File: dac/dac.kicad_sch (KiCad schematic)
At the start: 30 parts, among them J1 USB_B, U1 PCM2902, U2 SPX3819M5-L, Y1 12MHz

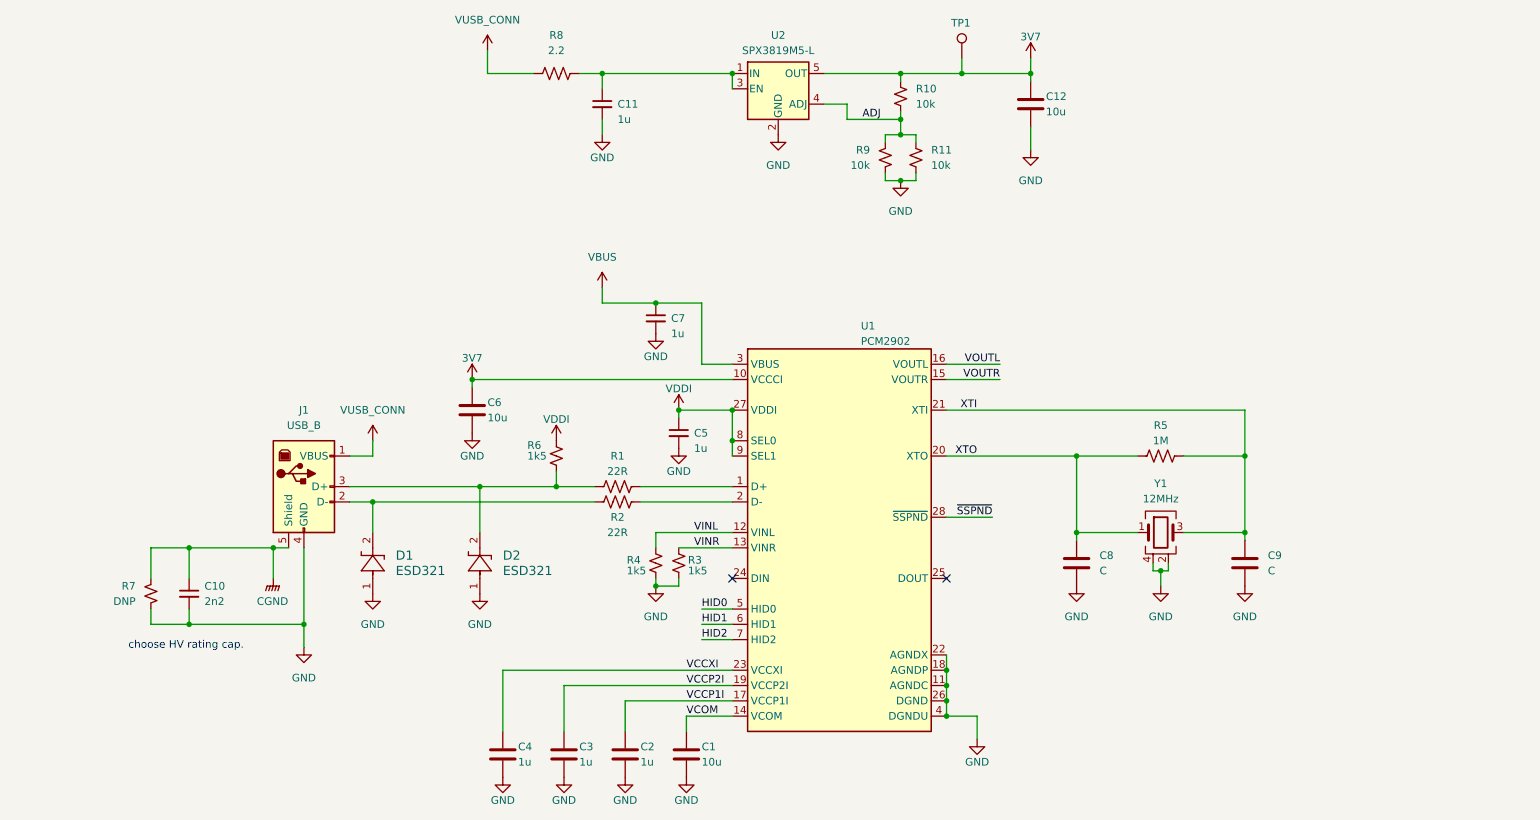
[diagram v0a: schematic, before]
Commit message: finished component placement, need to figure out header pinouts
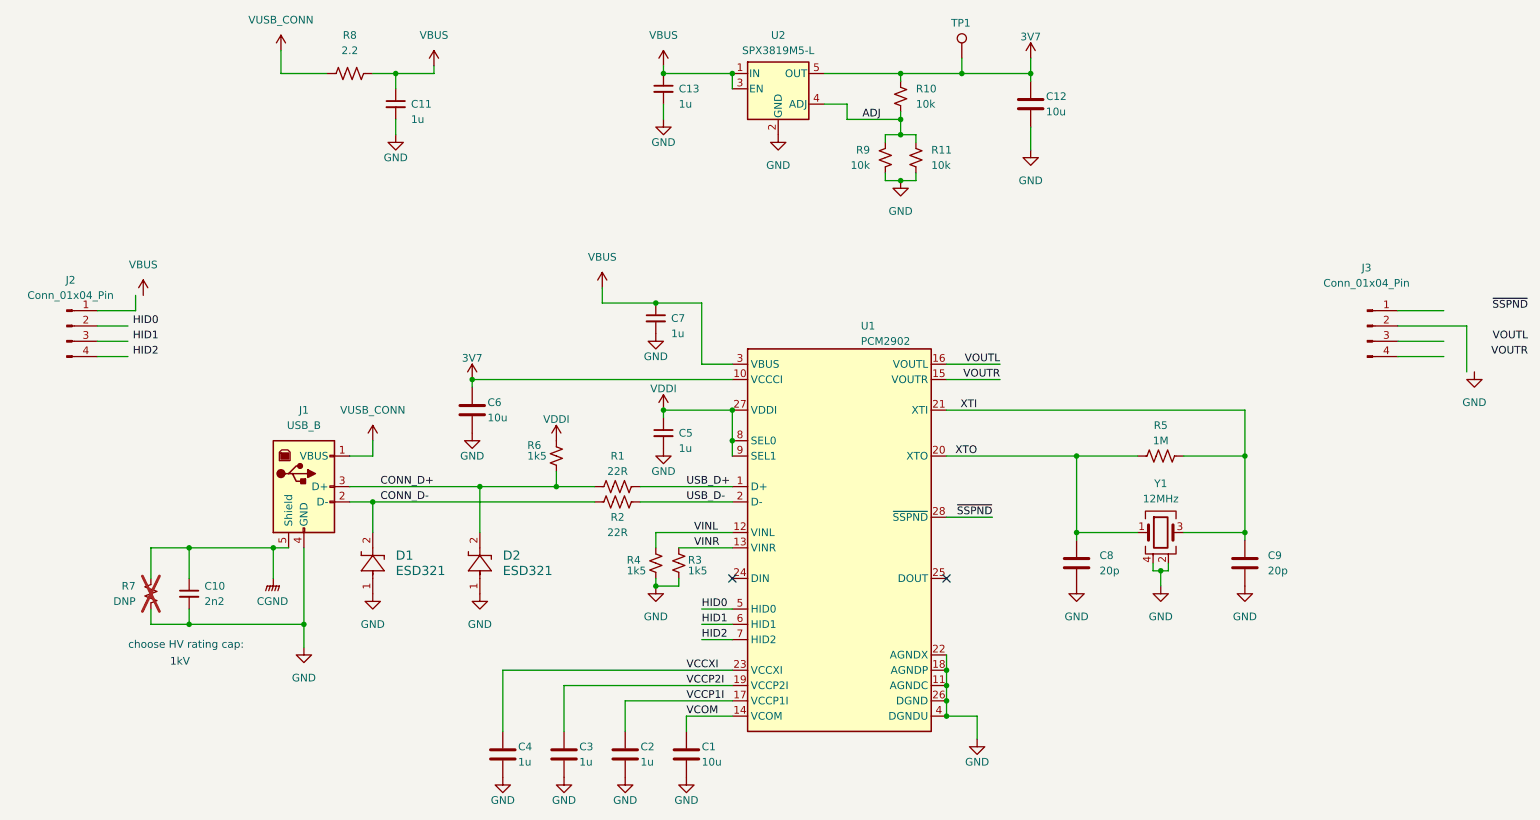
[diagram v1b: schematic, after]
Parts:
- added C13: 1u, Capacitor_SMD:C_0402_1005Metric_Pad0.74x0.62mm_HandSolder, symbol Device:C_Small
- added J2, J3: Conn_01x04_Pin, Connector_PinHeader_2.54mm:PinHeader_1x04_P2.54mm_Vertical, symbol Connector:Conn_01x04_Pin
- C1, C10, C12, C6: footprint (none) -> Capacitor_SMD:C_0805_2012Metric_Pad1.18x1.45mm_HandSolder
- C11, C2, C3, C4, C5, C7: footprint (none) -> Capacitor_SMD:C_0402_1005Metric_Pad0.74x0.62mm_HandSolder
- C8, C9: value C -> 20p; footprint (none) -> Capacitor_SMD:C_0402_1005Metric_Pad0.74x0.62mm_HandSolder
- J1: footprint (none) -> Connector_USB:USB_B_OST_USB-B1HSxx_Horizontal
- R1, R10, R11, R2, R3, R4, R5, R6, R9: footprint (none) -> Resistor_SMD:R_0402_1005Metric_Pad0.72x0.64mm_HandSolder
- R7: footprint (none) -> Resistor_SMD:R_0402_1005Metric_Pad0.72x0.64mm_HandSolder; now not fitted
- R8: footprint (none) -> Resistor_SMD:R_0603_1608Metric_Pad0.98x0.95mm_HandSolder
- TP1: footprint (none) -> TestPoint:TestPoint_Pad_D1.0mm
- Y1: footprint (none) -> ABM8:XTAL_ABM8-12.000MHZ-12-B1U-T
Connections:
- net GND: now also C13.2
- net VBUS: now also C11.1, R8.2, U2.1 (IN), U2.3 (EN), C13.1
- net USB_D+: now reaches R1.2, U1.1 (D+)
- net USB_D-: now reaches R2.2, U1.2 (D-)
- net CONN_D-: now reaches D1.2, J1.2 (D-), R2.1
- net CONN_D+: now reaches D2.2, J1.3 (D+), R1.1, R6.2
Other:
- note added: "1kV"
- note added: "choose HV rating cap:"
- note removed: "choose HV rating cap."
- moved on the sheet: C11, C5, R8

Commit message: layout is complete
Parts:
- added TP2: TestPoint, TestPoint:TestPoint_Pad_D1.0mm, symbol Connector:TestPoint
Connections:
- net GND: now also J2.2 (Pin_2)
- net HID0: now also J3.1 (Pin_1)
- net HID1: now also J3.2 (Pin_2)
- net HID2: now also J3.3 (Pin_3)
- net VBUS: now also J2.1 (Pin_1), TP2.1
- net VOUTL: now also J2.3 (Pin_3)
- net VOUTR: now also J2.4 (Pin_4)
- net ~{SSPND}: now also J3.4 (Pin_4)
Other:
- moved on the sheet: J2, J3

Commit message: final cleanup
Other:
- title: (none) -> PCM2903C DAC Breadboard Adapter
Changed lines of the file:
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@@
 	(generator_version "8.0")
 	(paper "A4")
+	(title_block
+		(title "PCM2903C DAC Breadboard Adapter")
+		(date "2024-10-10")
+		(rev "-")
+	)
 	(junction
 		(at 167.64 50.8)

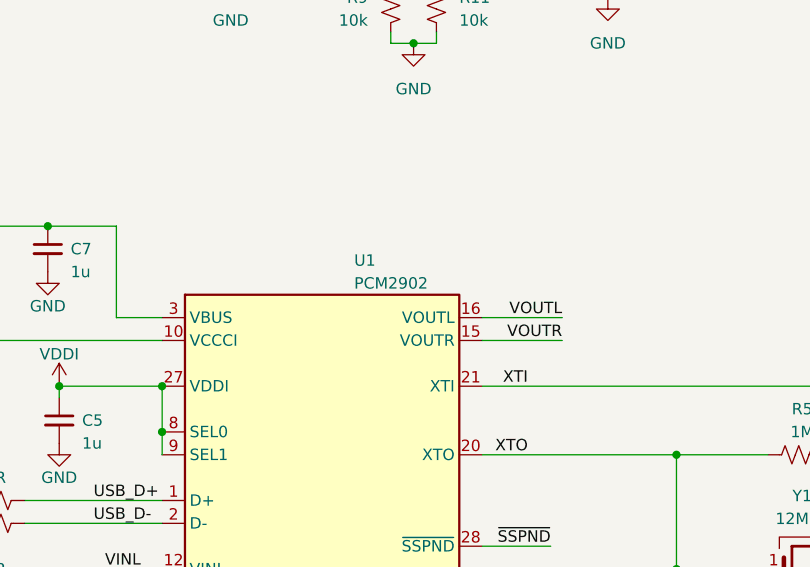
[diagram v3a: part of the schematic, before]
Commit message: changed U1 name to correct chip PCM2906C
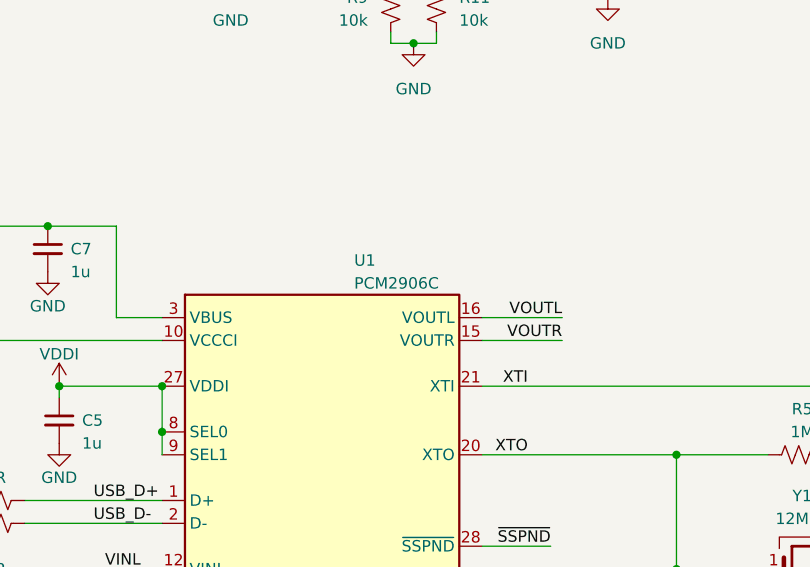
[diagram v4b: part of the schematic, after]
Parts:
- U1: value PCM2902 -> PCM2906C
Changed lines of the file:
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@@
 			)
 		)
-		(property "Value" "PCM2902"
+		(property "Value" "PCM2906C"
 			(at 161.036 77.47 0)
 			(effects
@@
 			)
 		)
-		(property "Datasheet" "http://www.ti.com/lit/ds/symlink/pcm2902c.pdf"
+		(property "Datasheet" ""
 			(at 168.2399 75.692 0)
 			(effects
